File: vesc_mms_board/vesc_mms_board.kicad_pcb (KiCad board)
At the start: 2 copper layers, 39 parts, among them J1 RJ45_LED_Shielded, J2 RJ45_LED_Shielded, J3 VCC_IN, J5 Conn_01x03, J6 Conn_01x05, SW1 SW_DIP_x02, U1 CH334R, Y1 12Mhz

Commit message: pcb created
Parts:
- removed the J5 at (140.4, 111.1)
- added J6: Conn_01x02, Connector_PinHeader_2.54mm:PinHeader_1x02_P2.54mm_Vertical, F.Cu at (126.7, 118.6)
- added J7: Conn_01x04, Connector_PinHeader_2.54mm:PinHeader_1x04_P2.54mm_Vertical, F.Cu at (112.2, 118.6)
- added kibuzzard-674E4526: G***, kibuzzard-674E4526, F.Cu at (128.2, 54.6)
- added kibuzzard-674E452F: G***, kibuzzard-674E452F, F.Cu at (92.0, 54.8)
- added kibuzzard-674E4620: G***, kibuzzard-674E4620, F.Cu at (92.6, 115.4)
- added kibuzzard-674E462A: G***, kibuzzard-674E462A, F.Cu at (116.2, 115.4)
- added kibuzzard-674E4631: G***, kibuzzard-674E4631, F.Cu at (125.4, 115.4)
- added kibuzzard-674E47A8: G***, kibuzzard-674E47A8, F.Cu at (83.4, 119.9)
- J5: renamed from J3; footprint Connector_AMASS:AMASS_XT60IPW-M_1x03_P7.20mm_Horizontal -> Connector_AMASS:AMASS_XT60PW-M_1x02_P7.20mm_Horizontal
- moved H10 90.6 mm to (102.0, 55.0)
- moved H6 87.4 mm to (84.0, 54.0)
- moved H9 75.9 mm to (118.0, 55.0)
- moved H5 71.3 mm to (84.0, 113.0)
- moved H1 67.8 mm to (87.5, 86.8), turned to 45 degrees
- moved H7 63.5 mm to (110.2, 64.2), turned to 45 degrees
- moved R2 62.7 mm to (90.8, 125.3), turned to 90 degrees
- moved R3 62.6 mm to (89.1, 125.3), turned to 90 degrees
- moved SW1 57.1 mm to (85.9, 122.6), turned to -90 degrees
- moved R12 56.9 mm to (100.5, 127.8)
- moved R11 56.7 mm to (100.5, 126.7), turned to 180 degrees
- moved R10 56.6 mm to (100.5, 125.7)
- moved R9 56.5 mm to (100.5, 124.7)
- moved C7 55.6 mm to (105.8, 121.0), turned to -90 degrees
- moved J4 55.5 mm to (97.8, 118.6), turned to -90 degrees
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- renumbered C4 to C2, C2 to C3, C3 to C4, H3 to H1, H2 to H10, H4 to H2, H5 to H3, H6 to H4, H7 to H5, H8 to H6, H9 to H7, H10 to H8, H1 to H9, J6 to J4, R7 to R1, R4 to R10, R5 to R11, R6 to R12, R8 to R13, R9 to R14, R1 to R2, R2 to R3, R10 to R4, R11 to R5, R12 to R6, R13 to R7, R14 to R8, R3 to R9
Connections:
- J1 pad 7: /CAN/USB_UPSTREAM_D+ -> USB_UPSTREAM_D+
- J1 pad 8: /CAN/USB_UPSTREAM_D- -> USB_UPSTREAM_D-
- J2 pad 7: /CAN/USB_DOWNSTREAM_D- -> USB_DOWNSTREAM_D-
- J2 pad 8: /CAN/USB_DOWNSTREAM_D+ -> USB_DOWNSTREAM_D+
- R11 pad 2: /USB/USB_DOWNSTREM_D- -> USB_DOWNSTREAM_D-
- R12 pad 1: /USB/USB_DOWNSTREM_D+ -> USB_DOWNSTREAM_D+
- R13 pad 1: /USB/USB_DOWNSTREAM_D+ -> USB_DOWNSTREAM_D+
- R13 pad 2: /USB/USB_UPSTREAM_D+ -> USB_UPSTREAM_D+
- R14 pad 1: /USB/USB_DOWNSTREAM_D- -> USB_DOWNSTREAM_D-
- R14 pad 2: /USB/USB_UPSTREAM_D- -> USB_UPSTREAM_D-
- U1 pad 10: /USB/USB_UPSTREAM_D- -> USB_UPSTREAM_D-
- U1 pad 11: /USB/USB_UPSTREAM_D+ -> USB_UPSTREAM_D+
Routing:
- net +12V: track 0.00 -> 108.3 mm, vias 0 -> 11
- net /CAN/CAN1-: track 0.00 -> 66.3 mm, vias 0 -> 2
- net /CAN/CAN2+: track 0.00 -> 64.3 mm, vias 0 -> 3
- net /CAN/CAN2-: track 0.00 -> 63.8 mm, vias 0 -> 2
- net /CAN/CAN1+: track 0.00 -> 62.3 mm, vias 0 -> 1
- net USB_DOWNSTREAM_D-: track 0.00 -> 37.1 mm, vias 0 -> 3
- net +5V: track 0.00 -> 35.0 mm
- net USB_DOWNSTREAM_D+: track 0.00 -> 32.5 mm, vias 0 -> 3
- net USB_UPSTREAM_D+: track 0.00 -> 30.5 mm
- net USB_UPSTREAM_D-: track 0.00 -> 27.7 mm
- net GND: track 0.00 -> 22.6 mm, vias 0 -> 18
- net /USB/USB_VESC_D+: track 0.00 -> 11.2 mm
- net /USB/USB_VESC_D-: track 0.00 -> 10.3 mm
- net Net-(C1-Pad1): track 0.00 -> 9.34 mm
- net Net-(C2-Pad1): track 0.00 -> 9.09 mm
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- added copper zone on B.Cu, net GND
- added copper zone on F.Cu, net GND
- added copper zone on B.Cu, net VCC
- added copper zone on F.Cu, net VCC
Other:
- board outline added: 60 x 100 mm
- board text added: "BYPASS USB HUB"
- board text added: "CAN1"
- board text added: "CAN2"
- board text added: "Do NOT solder usb hub if bypass is used"
- board text added: "SELECT only one CANx!"

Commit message: fianl
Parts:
- added kibuzzard-673147F0: G***, kibuzzard-673147F0, B.Cu at (110.5, 146.3)
- added kibuzzard-67314807: G***, kibuzzard-67314807, B.Cu at (90.9, 146.3)
- added kibuzzard-6754762D: G***, kibuzzard-6754762D, F.Cu at (111.1, 130.4)
- H1, H2, H4, H7: footprint MountingHole:MountingHole_3.5mm -> MountingHole:MountingHole_4.3mm_M4
- moved H7 33.0 mm to (93.0, 92.4), turned to 135 degrees
- moved H1 31.8 mm to (110.0, 109.3), turned to 135 degrees
- moved H2 25.5 mm to (110.0, 75.4), turned to 135 degrees
- moved H4 23.9 mm to (127.0, 92.4), turned to 135 degrees
- moved kibuzzard-674E4526 12.4 mm to (117.9, 61.5)
- moved kibuzzard-674E452F 12.3 mm to (102.1, 61.8)
- moved kibuzzard-674E4620 2.22 mm to (93.9, 113.6)
- moved J4 1.78 mm to (99.6, 118.6)
- moved kibuzzard-674E462A 1.73 mm to (116.5, 113.7)
- moved kibuzzard-674E4631 1.71 mm to (125.6, 113.7)
- moved kibuzzard-674E47A8 1.02 mm to (84.4, 119.9)
- moved H5 1.00 mm to (84.0, 114.0)
- moved J6 0.61 mm to (127.3, 118.5)
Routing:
- net +5V: track 35.0 -> 31.5 mm
- net USB_DOWNSTREAM_D+: track 32.5 -> 35.6 mm
- net USB_DOWNSTREAM_D-: track 37.1 -> 39.0 mm
- net /USB/USB_VESC_D+: track 11.2 -> 10.3 mm
- net /CAN/CAN1+: track 62.3 -> 63.2 mm
- net /USB/USB_VESC_D-: track 10.3 -> 9.39 mm
- net GND: track 22.6 -> 22.9 mm, vias 18 -> 20
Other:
- outline, holes or cut-outs redrawn
- board text added: "12V"
- board text added: "3.2mm"
- board text added: "30mm FAN (3010)"
- board text added: "52mm"
- board text added: "5V"
- board text added: "60mm"
- board text added: "C1+"
- board text added: "C1-"
- board text added: "C2+"
- board text added: "C2-"
- board text added: "CH"
- board text added: "CL"
- board text added: "D+"
- board text added: "D-"
- board text added: "GND"
- board text added: "Voltage rating 12-50V"

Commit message: cehnaged leyour added vias
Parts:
- removed C1, C2: 10n, Capacitor_SMD:C_0402_1005Metric
- removed R1, R4: 33k, Resistor_SMD:R_0402_1005Metric
- added R17: 1k, Resistor_SMD:R_0402_1005Metric, F.Cu at (94.5, 131.2)
- added R18: 1k, Resistor_SMD:R_0402_1005Metric, F.Cu at (102.6, 131.2)
- C4: footprint Capacitor_SMD:C_0603_1608Metric -> Capacitor_SMD:C_0402_1005Metric
- moved kibuzzard-674E47A8 34.8 mm to (118.5, 113.1)
- moved SW1 34.6 mm to (119.8, 115.6)
- moved kibuzzard-674E4631 23.1 mm to (106.8, 127.2)
- moved R3 23.1 mm to (112.0, 122.3)
- moved R2 23.0 mm to (113.6, 122.3)
- moved J6 22.4 mm to (108.0, 129.8)
- moved C4 12.5 mm to (91.9, 121.9)
- moved R12 12.2 mm to (88.3, 128.5)
- moved R11 12.2 mm to (88.3, 127.4)
- moved R9 12.2 mm to (88.3, 125.4)
- moved Y1 12.2 mm to (100.0, 123.6)
- moved R10 12.2 mm to (88.3, 126.4)
- moved U1 12.2 mm to (93.3, 125.6)
- moved R8 12.1 mm to (105.3, 122.3)
- moved C3 12.0 mm to (90.7, 121.3)
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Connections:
- J1 pad 11: unconnected-(J1-Pad11) -> GND
- J1 pad 12: unconnected-(J1-Pad12) -> Net-(J1-Pad12)
- J1 pad 7: USB_UPSTREAM_D+ -> USB_UPSTREAM_D-
- J1 pad 8: USB_UPSTREAM_D- -> USB_UPSTREAM_D+
- J1 pad SH: Net-(C1-Pad1) -> GND
- J2 pad 10: unconnected-(J2-Pad10) -> Net-(J2-Pad10)
- J2 pad 9: unconnected-(J2-Pad9) -> GND
- J2 pad SH: Net-(C2-Pad1) -> GND
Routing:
- net +12V: track 108.6 -> 38.1 mm, vias 11 -> 0
- net /CAN/CAN2-: track 64.2 -> 88.1 mm
- net GND: track 22.9 -> 1.81 mm, vias 20 -> 471
- net /CAN/CAN2+: track 64.2 -> 83.9 mm, vias 3 -> 1
- net /CAN/CAN1+: track 63.2 -> 80.9 mm, vias 1 -> 2
- net USB_DOWNSTREAM_D-: track 39.0 -> 21.8 mm, vias 3 -> 2
- net USB_DOWNSTREAM_D+: track 35.6 -> 20.0 mm, vias 3 -> 2
- net /USB/USB_VESC_D-: track 9.39 -> 23.2 mm
- net /USB/USB_VESC_D+: track 10.3 -> 23.9 mm
- net USB_UPSTREAM_D-: track 27.7 -> 37.3 mm, vias 0 -> 3
- net Net-(C1-Pad1): track 9.34 -> 0.00 mm
- net Net-(C2-Pad1): track 9.09 -> 0.00 mm
- net USB_UPSTREAM_D+: track 30.5 -> 38.1 mm, vias 0 -> 3
- net /CAN/CAN1-: track 66.3 -> 73.8 mm, vias 2 -> 3
- net +5V: track 31.5 -> 38.3 mm
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
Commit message: update tetx
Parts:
- removed kibuzzard-674E47A8: G***, kibuzzard-674E47A8
- added kibuzzard-675D9C67: G***, kibuzzard-675D9C67, F.Cu at (118.6, 111.1)
- added kibuzzard-675D9C73: G***, kibuzzard-675D9C73, F.Cu at (120.9, 113.4)
- added kibuzzard-675D9C7D: G***, kibuzzard-675D9C7D, F.Cu at (116.4, 113.4)
- added kibuzzard-675D9CCD: G***, kibuzzard-675D9CCD, F.Cu at (122.7, 119.3)
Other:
- board text added: "SOLDER ONLY ONE GROUP"
- board text removed: "SELECT only one CANx!"

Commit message: updaet text
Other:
- board text added: "R13"
- board text added: "R14"
- board text added: "USB BYPASS BLOCK DIAGRAM"
- board text added: "USB HUB"
- board text added: "USB IN"
- board text added: "USB OUT"

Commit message: updarte readme final desing rev a
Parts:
- added C1: 10u, Capacitor_SMD:C_0603_1608Metric, F.Cu at (104.0, 127.1)
- added C2: 100n, Capacitor_SMD:C_0402_1005Metric, F.Cu at (110.7, 131.1)
- moved kibuzzard-674E4631 6.32 mm to (113.1, 127.7)
- moved kibuzzard-6754762D 1.81 mm to (117.0, 130.3)
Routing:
- net +12V: track 38.1 -> 45.5 mm
- net GND: vias 471 -> 479

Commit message: Update rev 2.0, added step files
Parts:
- removed H1: MountingHole, MountingHole:MountingHole_4.3mm_M4
- removed J7: Conn_01x04, Connector_PinHeader_2.54mm:PinHeader_1x04_P2.54mm_Vertical
- added J3: Conn_01x04, Connector_JST:JST_XH_B4B-XH-A_1x04_P2.50mm_Vertical, F.Cu at (106.7, 115.2)
- C1, C2: moved to B.Cu
- J4: footprint Connector_PinHeader_2.54mm:PinHeader_1x05_P2.54mm_Vertical -> Connector_JST:JST_XH_B5B-XH-A_1x05_P2.50mm_Vertical
- J6: footprint Connector_PinHeader_2.54mm:PinHeader_1x02_P2.54mm_Vertical -> Connector_JST:JST_XH_B2B-XH-A_1x02_P2.50mm_Vertical
- moved kibuzzard-674E4631 14.4 mm to (98.8, 128.8)
- moved J4 10.4 mm to (90.7, 115.2), turned to 0 degrees
- moved kibuzzard-675D9C67 3.20 mm to (121.7, 112.0)
- moved kibuzzard-674E462A 3.09 mm to (110.1, 111.1)
- moved kibuzzard-675D9C7D 3.08 mm to (119.5, 113.5)
- moved kibuzzard-675D9CCD 2.77 mm to (125.5, 119.2)
- moved kibuzzard-675D9C73 2.72 mm to (123.6, 113.5)
- moved SW1 2.26 mm to (122.1, 115.6)
- moved kibuzzard-674E4620 2.23 mm to (95.8, 111.3)
- moved R18 1.43 mm to (101.2, 131.2)
- moved J5 1.15 mm to (134.8, 131.6)
- moved J6 1.05 mm to (107.6, 128.8), turned to 180 degrees
- moved C1 0.64 mm to (104.5, 126.7)
- moved C2 0.50 mm to (110.2, 131.2)
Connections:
- J4 pad 1: +5V -> GND
- J4 pad 2: /USB/USB_VESC_D- -> GND
- J4 pad 4: GND -> /USB/USB_VESC_D-
- J4 pad 5: GND -> +5V
- J6 pad 1: +12V -> GND
- J6 pad 2: GND -> +12V
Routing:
- net +5V: track 38.3 -> 41.8 mm
- net /CAN/CAN+: track 13.8 -> 17.1 mm
- net /CAN/CAN-: track 14.1 -> 17.3 mm
- net /CAN/CAN2+: track 83.9 -> 80.9 mm
- net Net-(R2-Pad2): track 8.74 -> 11.7 mm
- net Net-(R3-Pad2): track 8.07 -> 10.7 mm
- net +12V: track 45.5 -> 48.1 mm
- net /CAN/CAN2-: track 88.1 -> 86.1 mm
- net /CAN/CAN1-: track 73.8 -> 72.8 mm
- net Net-(J1-Pad12): track 2.29 -> 2.90 mm
- net GND: track 1.81 -> 2.23 mm, vias 479 -> 723
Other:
- board size 60 x 100 mm -> 60 x 104.5 mm

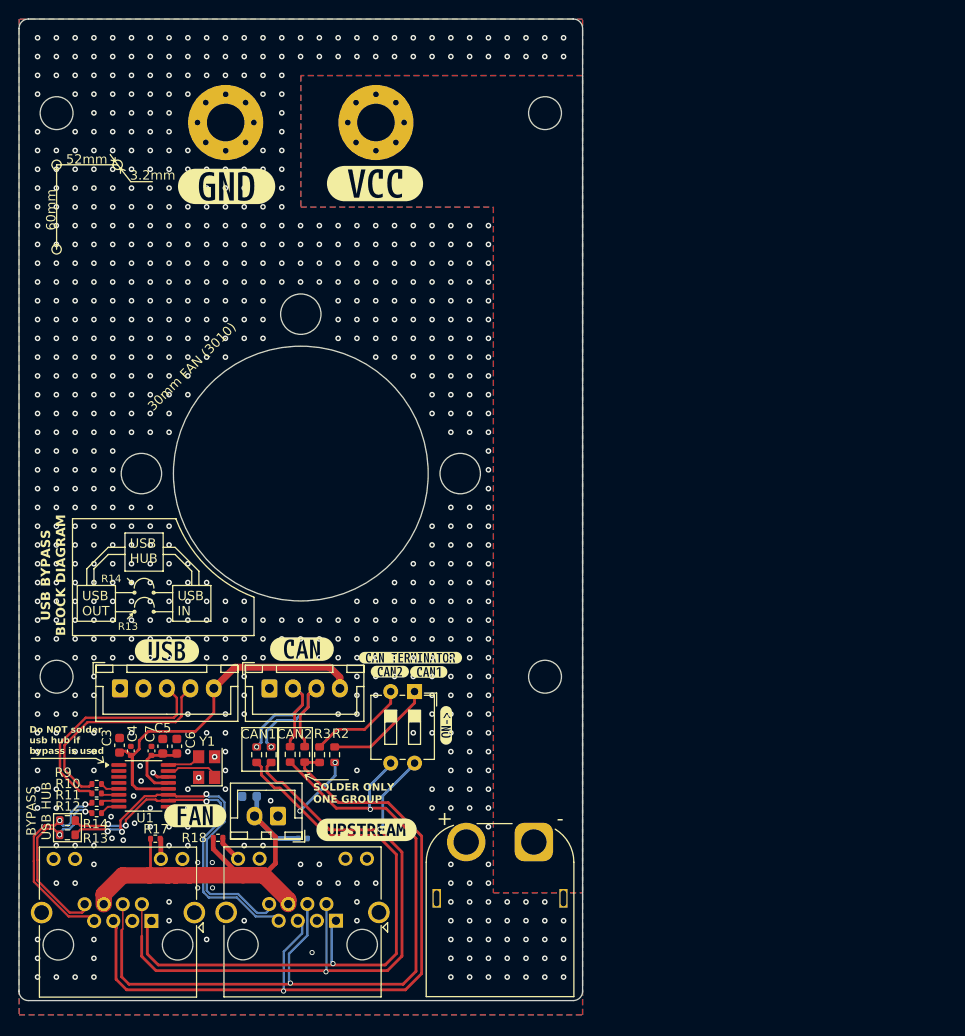
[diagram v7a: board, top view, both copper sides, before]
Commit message: fixed problem with xt60
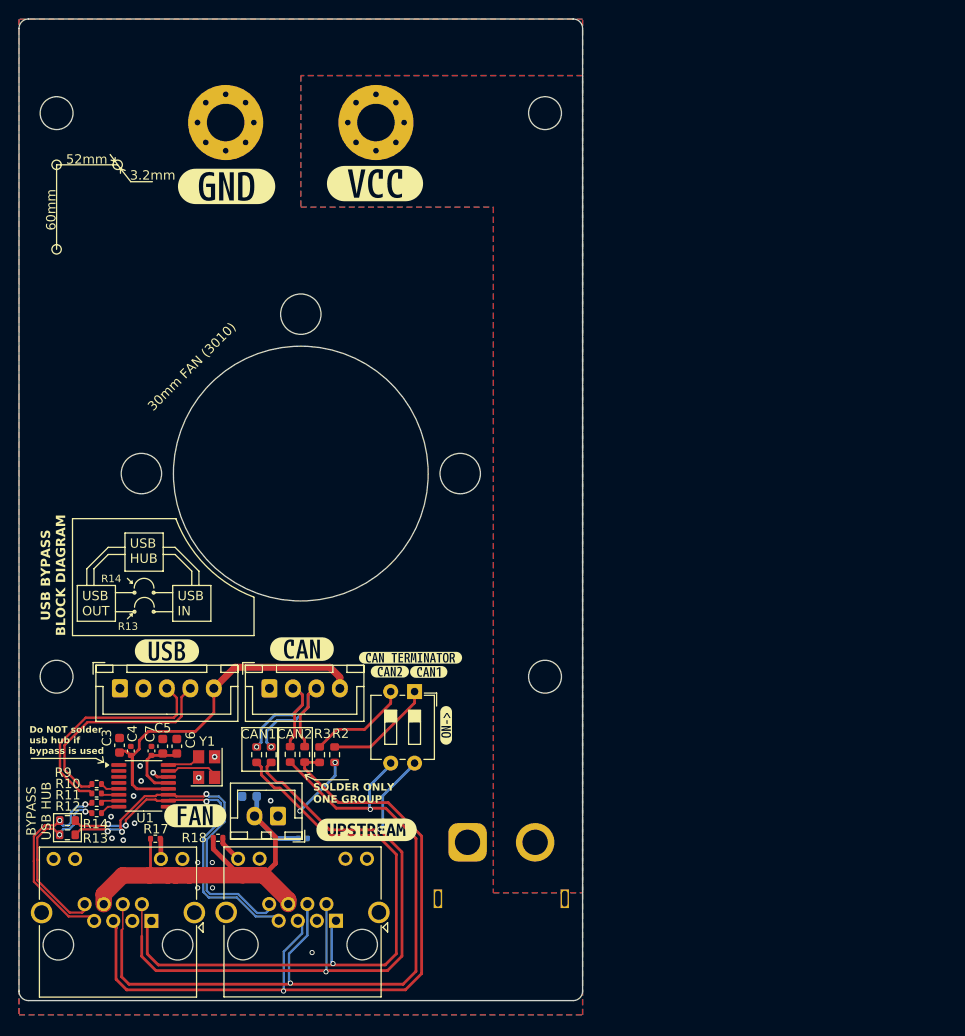
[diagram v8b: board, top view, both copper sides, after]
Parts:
- J5: moved to B.Cu
- moved J5 7.06 mm to (127.8, 131.6), turned to 0 degrees
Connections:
- J5 pad 1: VCC -> GND
- J5 pad 2: GND -> VCC
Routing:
- net GND: vias 723 -> 16
